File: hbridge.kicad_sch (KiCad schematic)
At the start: 19 parts, among them J1 Conn_01x04_Male, J2 Screw_Terminal_01x03, Q1 2N7000, Q2 2N7000, Q3 2N3904, Q4 2N3906, Q5 2N3904, Q6 2N3906, Q7 STP20NF06, Q8 STP20NF06

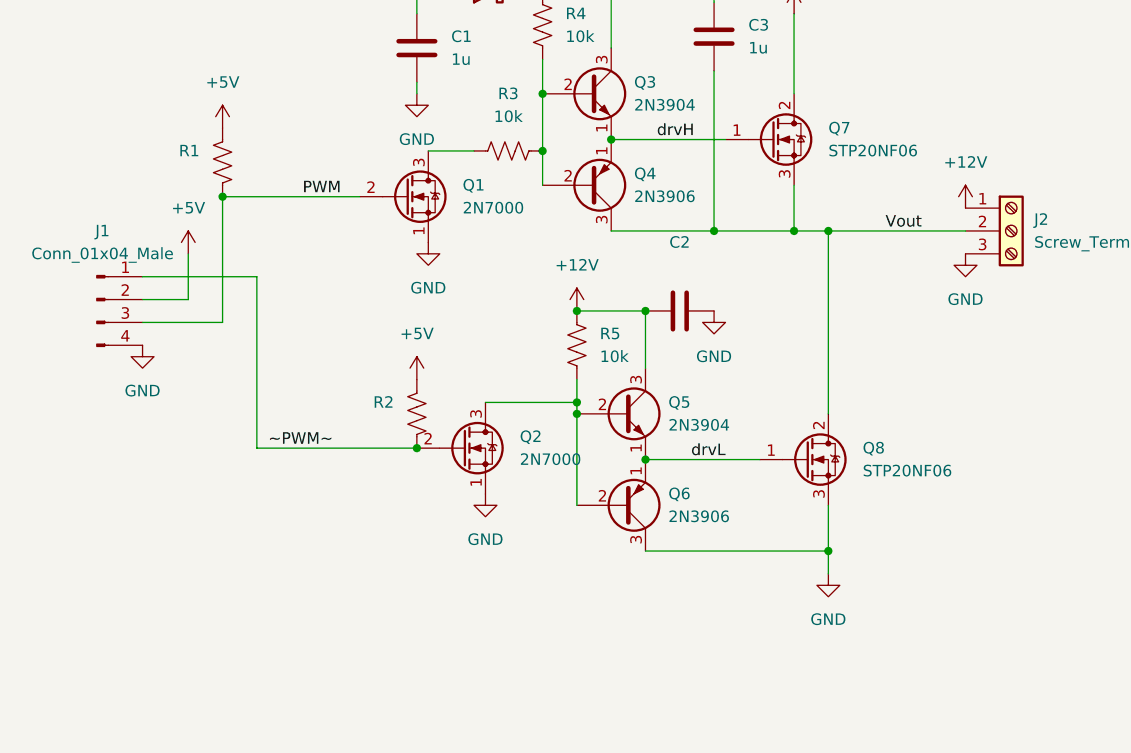
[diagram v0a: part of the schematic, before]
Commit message: Tied Q4 collector to ground to turn off Q7 harder. Moved traces so entire back side is ground plane.
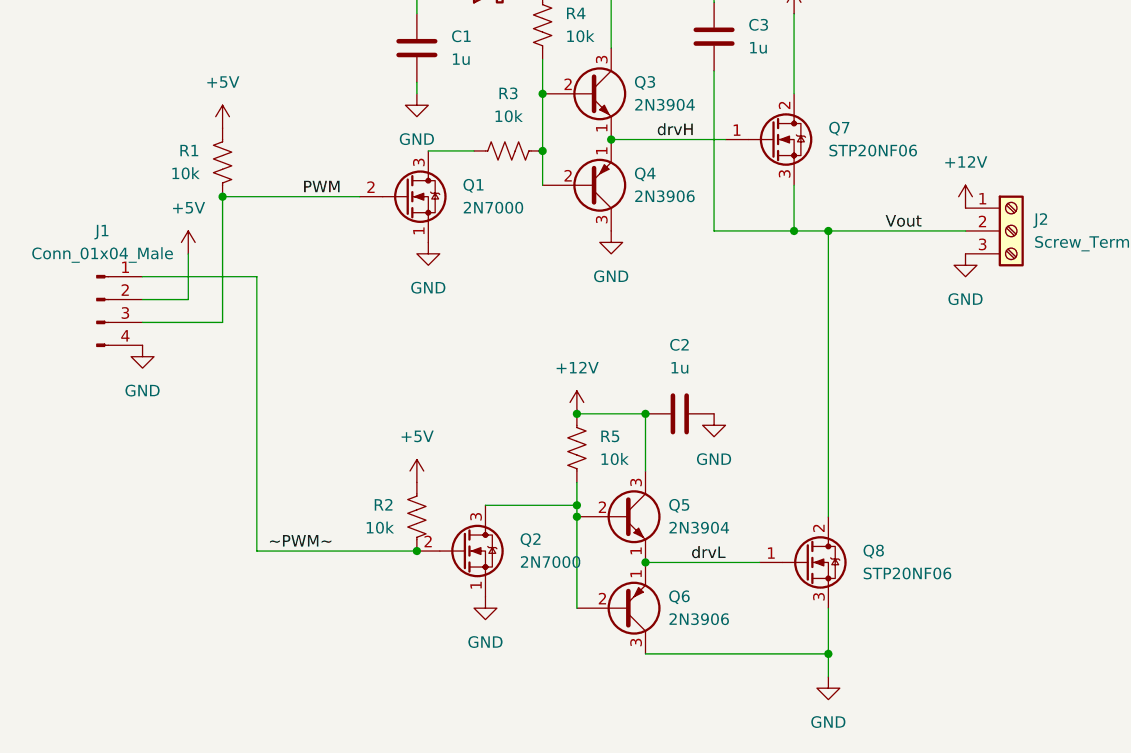
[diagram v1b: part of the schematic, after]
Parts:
- C2: value (none) -> 1u
- R1, R2: value (none) -> 10k
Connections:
- net GND: now also Q4.3 (C)
- net Vout: no longer Q4.3 (C)
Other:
- moved on the sheet: C2, Q2, Q5, Q6, Q8, R2, R5

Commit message: Removed R3 to turn off Q7 harder
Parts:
- removed R3: 10k, Resistor_THT:R_Axial_DIN0204_L3.6mm_D1.6mm_P2.54mm_Vertical, symbol Device:R_US
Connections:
- net at Q1.3 (D): now also Q3.2 (B), Q4.2 (B), R4.2
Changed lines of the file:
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@@
   (junction (at 156.21 120.65) (diameter 0) (color 0 0 0 0)
   )
+  (junction (at 152.4 90.17) (diameter 0) (color 0 0 0 0)
+  )
+  (junction (at 109.22 96.52) (diameter 0) (color 0 0 0 0)
+  )
+  (junction (at 176.53 100.33) (diameter 0) (color 0 0 0 0)
+  )
   (junction (at 144.78 91.44) (diameter 0) (color 0 0 0 0)
   )
-  (junction (at 152.4 90.17) (diameter 0) (color 0 0 0 0)
-  )
-  (junction (at 109.22 96.52) (diameter 0) (color 0 0 0 0)
-  )
-  (junction (at 176.53 100.33) (diameter 0) (color 0 0 0 0)
-  )
   (junction (at 148.59 120.65) (diameter 0) (color 0 0 0 0)
   )
@@
     (stroke (width 0) (type default) (color 0 0 0 0))
   )
-  (wire (pts (xy 132.08 91.44) (xy 137.16 91.44))
+  (wire (pts (xy 132.08 91.44) (xy 144.78 91.44))
+    (stroke (width 0) (type default) (color 0 0 0 0))
+  )
+  (wire (pts (xy 144.78 91.44) (xy 144.78 95.25))
     (stroke (width 0) (type default) (color 0 0 0 0))
   )
@@
     (stroke (width 0) (type default) (color 0 0 0 0))
   )
-  (wire (pts (xy 144.78 91.44) (xy 144.78 95.25))
+  (wire (pts (xy 144.78 85.09) (xy 144.78 91.44))
     (stroke (width 0) (type default) (color 0 0 0 0))
   )
   (wire (pts (xy 144.78 73.66) (xy 152.4 73.66))
-    (stroke (width 0) (type default) (color 0 0 0 0))
-  )
-  (wire (pts (xy 144.78 85.09) (xy 144.78 91.44))
     (stroke (width 0) (type default) (color 0 0 0 0))
   )
@@
     (pin "3")
   )
-  (symbol (lib_id "Device:R_US") (at 140.97 91.44 90) (unit 1)
-    (in_bom yes) (on_board yes) (fields_autoplaced)
-    (property "Reference" "R3" (id 0) (at 140.97 85.09 90))
-    (property "Value" "10k" (id 1) (at 140.97 87.63 90))
-    (property "Footprint" "Resistor_THT:R_Axial_DIN0204_L3.6mm_D1.6mm_P2.54mm_Vertical" (id 2) (at 141.224 90.424 90)
-      (effects (font (size 1.27 1.27)) hide)
-    )
-    (property "Datasheet" "~" (id 3) (at 140.97 91.44 0)
-      (effects (font (size 1.27 1.27)) hide)
-    )
-    (pin "1")
-    (pin "2")
-  )
   (symbol (lib_id "Device:R_US") (at 130.81 132.08 0) (mirror x) (unit 1)
     (in_bom yes) (on_board yes) (fields_autoplaced)
@@
       (reference "R2") (unit 1) (value "10k") (footprint "Resistor_THT:R_Axial_DIN0204_L3.6mm_D1.6mm_P2.54mm_Vertical")
     )
-    (path "/79db6aae-f78b-4231-a9f0-2ef15b641e87"
-      (reference "R3") (unit 1) (value "10k") (footprint "Resistor_THT:R_Axial_DIN0204_L3.6mm_D1.6mm_P2.54mm_Vertical")
-    )
     (path "/d37c9a21-a75d-4c2f-950c-c4469540ead5"

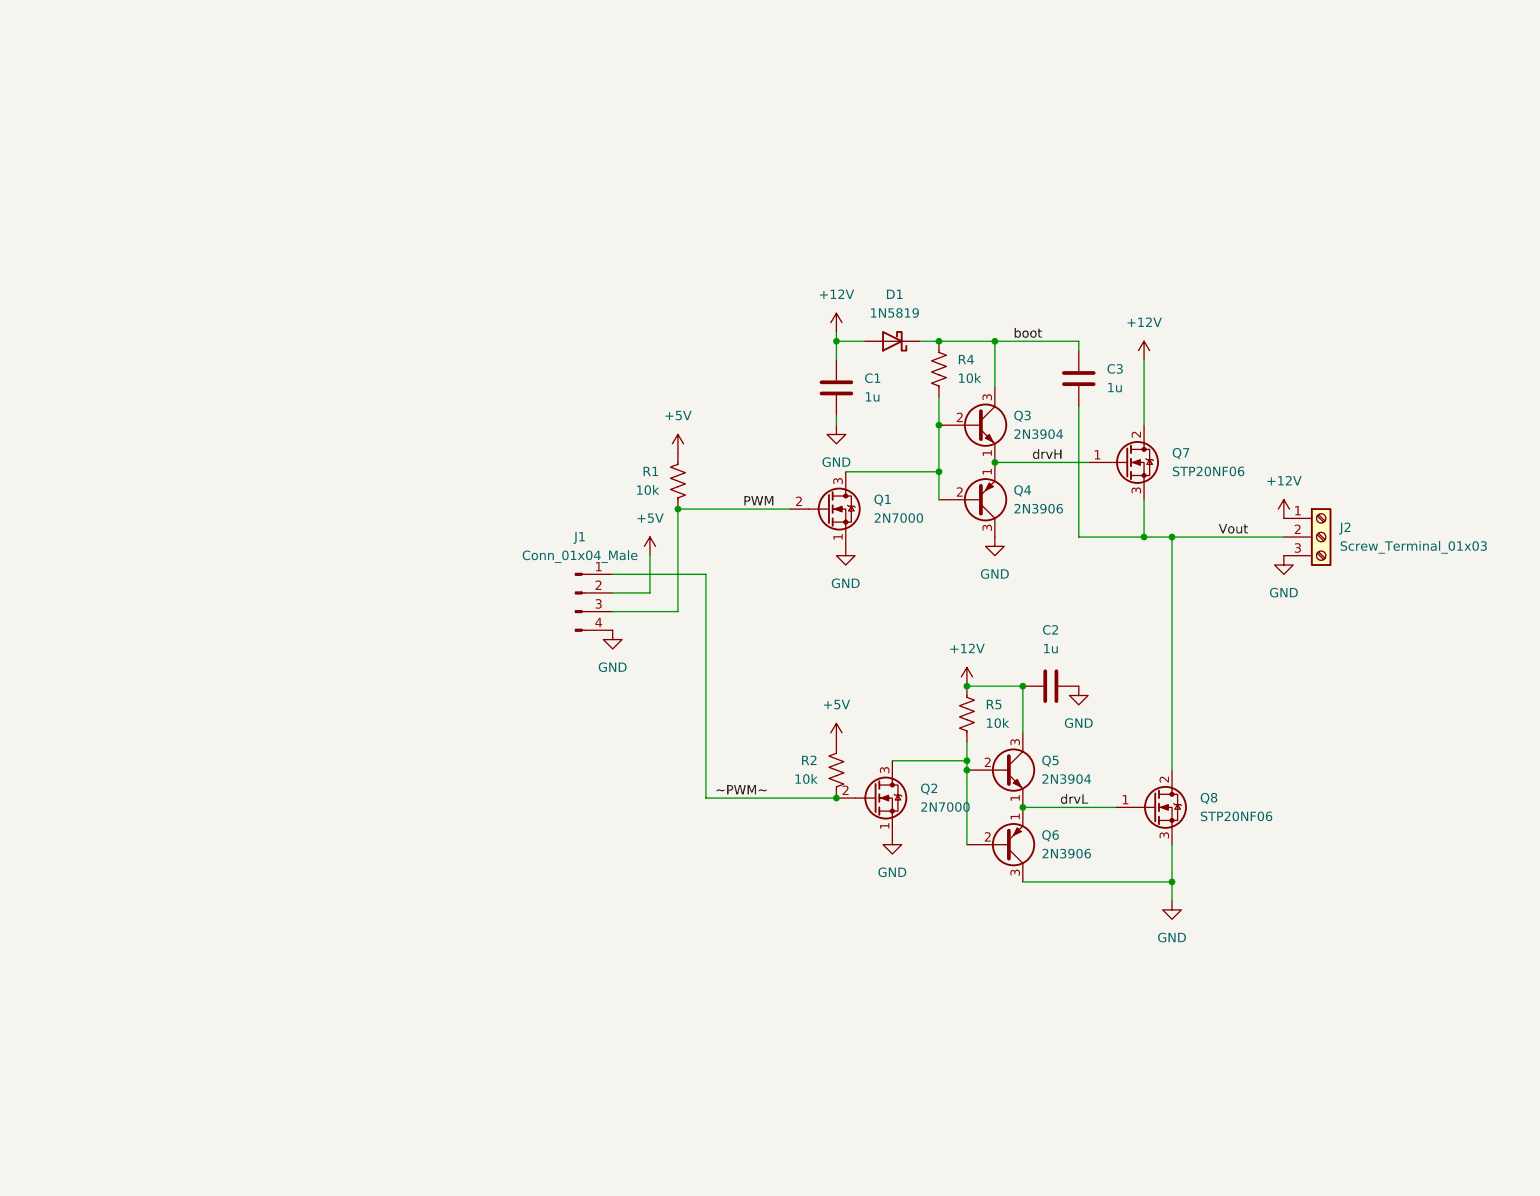
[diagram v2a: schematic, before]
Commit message: Added second half-bridge to make h-bridge. Not routed yet
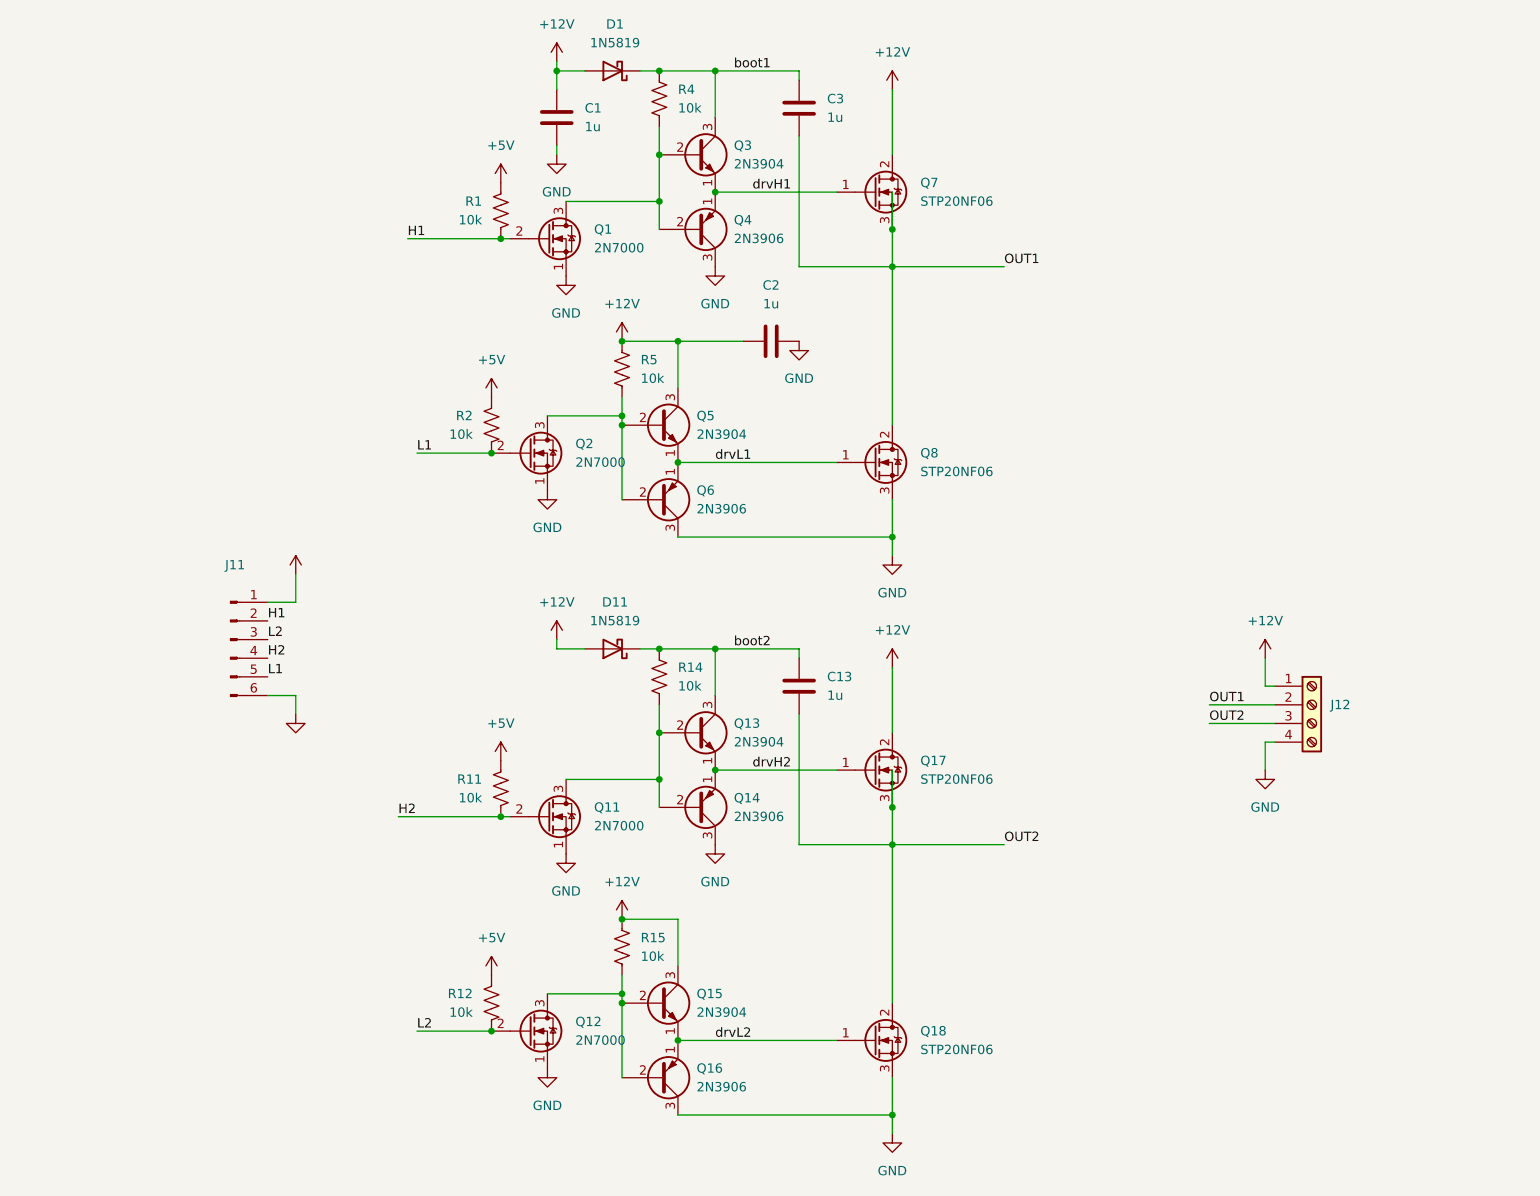
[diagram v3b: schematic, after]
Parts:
- removed J1: Conn_01x04_Male, Connector_PinHeader_2.54mm:PinHeader_1x04_P2.54mm_Vertical, symbol Connector:Conn_01x04_Male
- removed J2: Screw_Terminal_01x03, Connector_Phoenix_MC:PhoenixContact_MCV_1,5_3-G-3.5_1x03_P3.50mm_Vertical, symbol Connector:Screw_Terminal_01x03
- added C13: 1u, Capacitor_THT:C_Disc_D3.0mm_W1.6mm_P2.50mm, symbol Device:C
- added D11: 1N5819, Diode_THT:D_DO-41_SOD81_P5.08mm_Vertical_AnodeUp, symbol Diode:1N5819
- added J11: (no value), symbol Connector:Conn_01x06_Male
- added J12: (no value), symbol Connector:Screw_Terminal_01x04
- added Q11, Q12: 2N7000, Package_TO_SOT_THT:TO-92_Inline, symbol Transistor_FET:2N7000
- added Q13, Q15: 2N3904, Package_TO_SOT_THT:TO-92_Inline, symbol Transistor_BJT:2N3904
- added Q14, Q16: 2N3906, Package_TO_SOT_THT:TO-92_Inline, symbol Transistor_BJT:2N3906
- added Q17, Q18: STP20NF06, Package_TO_SOT_THT:TO-220-3_Vertical, symbol Device:Q_NMOS_GDS
- added R11, R12, R14, R15: 10k, Resistor_THT:R_Axial_DIN0204_L3.6mm_D1.6mm_P2.54mm_Vertical, symbol Device:R_US
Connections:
- net +12V: now also D11.2 (A), J12.1 (Pin_1), Q15.3 (C), Q17.2 (D), R15.1
- net +5V: now also J11.1 (Pin_1), R11.2, R12.2
- net GND: now also J11.6 (Pin_6), J12.4 (Pin_4), Q11.1 (S), Q12.1 (S), Q14.3 (C), Q16.3 (C), Q18.3 (S)
- net PWM renamed H1
- net H1: now also J11.2 (Pin_2)
- net Vout renamed OUT1
- net OUT1: now also J12.2 (Pin_2)
- net boot renamed boot1
- net drvH renamed drvH1
- net drvL renamed drvL1
- net ~PWM~ renamed L1
- net L1: now also J11.5 (Pin_5)
- new net: Q11.3 (D), Q13.2 (B), Q14.2 (B), R14.2
- new net: Q12.3 (D), Q15.2 (B), Q16.2 (B), R15.2
- new net H2: J11.4 (Pin_4), Q11.2 (G), R11.1
- new net L2: J11.3 (Pin_3), Q12.2 (G), R12.1
- new net OUT2: C13.2, J12.3 (Pin_3), Q17.3 (S), Q18.2 (D)
- new net boot2: C13.1, D11.1 (K), Q13.3 (C), R14.1
- new net drvH2: Q13.1 (E), Q14.1 (E), Q17.1 (G)
- new net drvL2: Q15.1 (E), Q16.1 (E), Q18.1 (G)
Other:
- moved on the sheet: C1, C2, C3, D1, Q1, Q2, Q3, Q4, Q5, Q6, Q7, Q8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

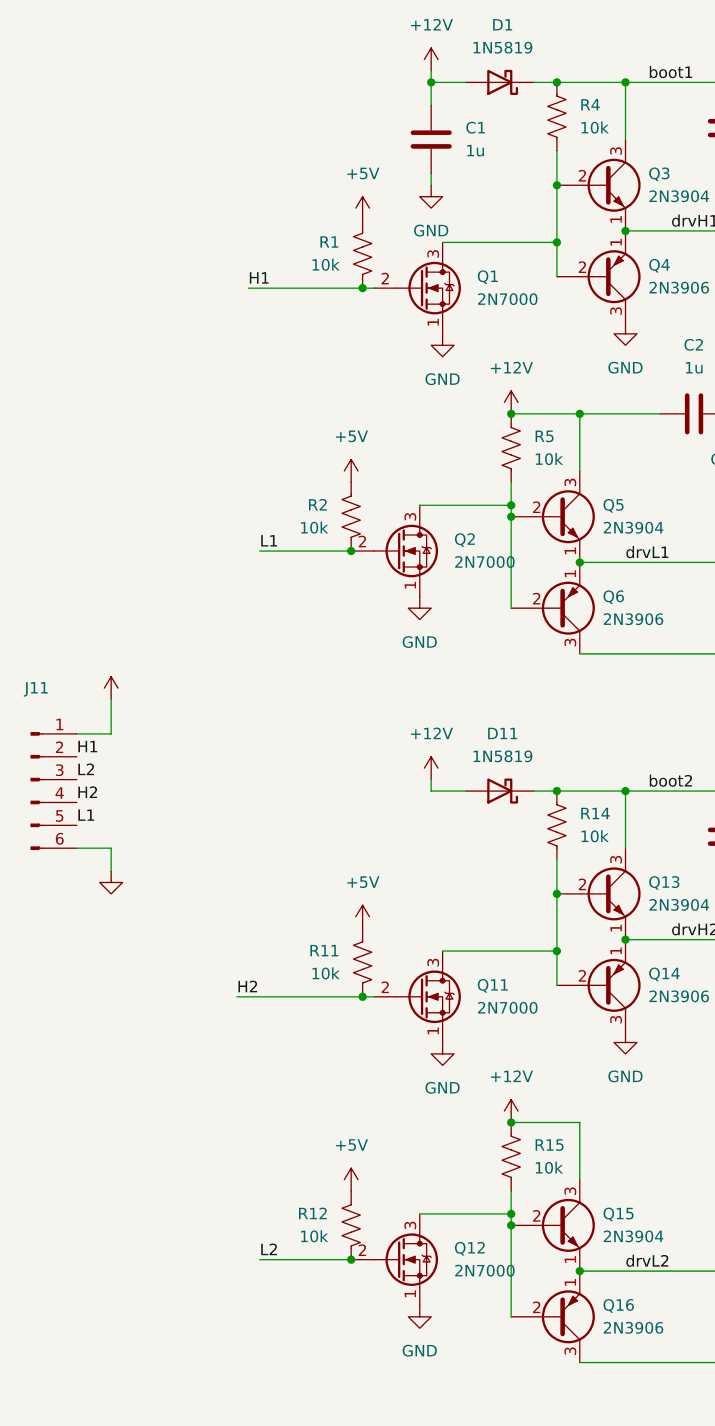
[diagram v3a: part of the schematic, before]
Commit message: More compact layout using smd resistors and capacitors
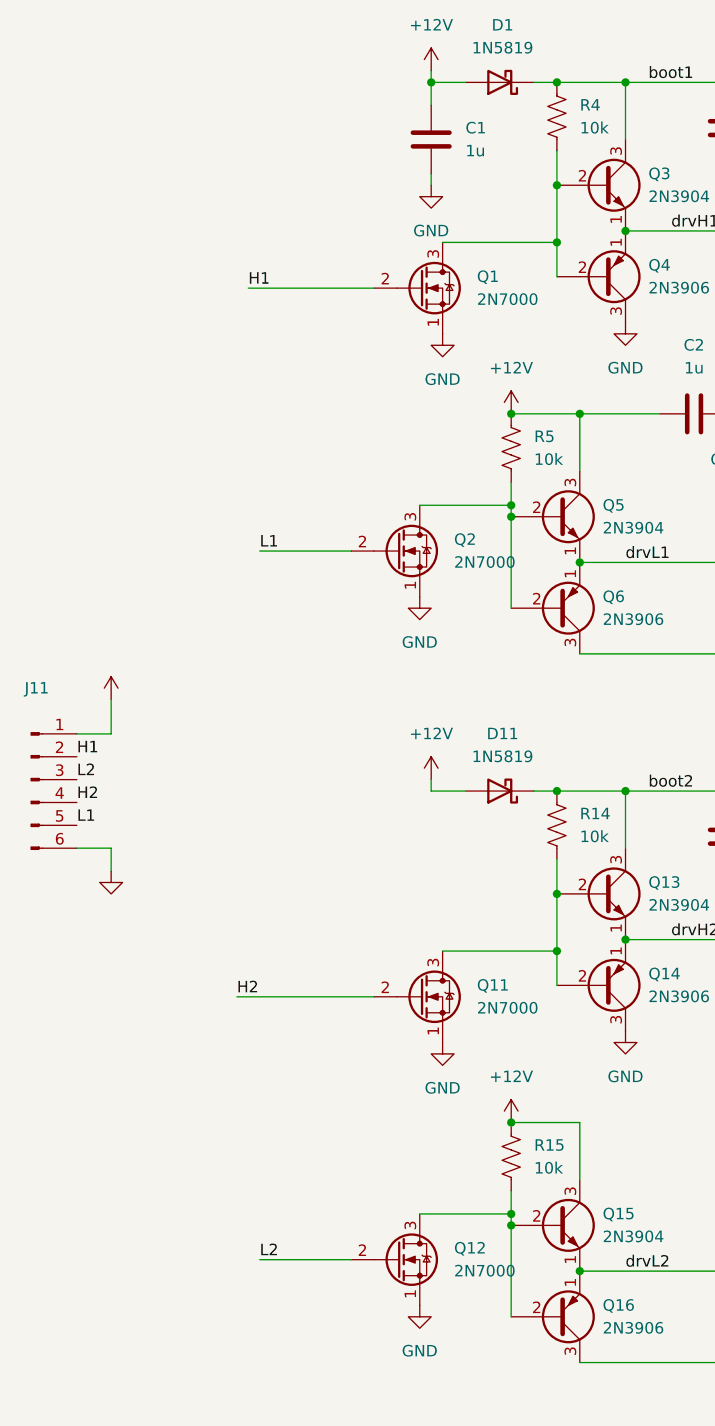
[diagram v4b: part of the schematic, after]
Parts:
- removed R1, R11, R12, R2: 10k, Resistor_THT:R_Axial_DIN0204_L3.6mm_D1.6mm_P2.54mm_Vertical, symbol Device:R_US
- C1, C13, C2, C3: footprint Capacitor_THT:C_Disc_D3.0mm_W1.6mm_P2.50mm -> (none)
- R14, R15, R4, R5: footprint Resistor_THT:R_Axial_DIN0204_L3.6mm_D1.6mm_P2.54mm_Vertical -> (none)
